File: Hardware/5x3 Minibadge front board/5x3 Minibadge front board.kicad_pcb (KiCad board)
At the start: 2 copper layers, 142.2 x 91.4 mm, 16 parts, among them J1 Board to Board

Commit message: Change board size + mounting holes
still need to finish re-routing the front plate
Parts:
- added J1: Board to Board, Connector_PinHeader_2.54mm:PinHeader_2x05_P2.54mm_Vertical_SMD, B.Cu at (213.4, 96.5)
- added REF**: MountingHole_2.2mm_M2, MountingHole:MountingHole_2.2mm_M2, F.Cu at (92.7, 57.1)
- added REF**: MountingHole_2.2mm_M2, MountingHole:MountingHole_2.2mm_M2, F.Cu at (157.5, 138.4)
- added REF**: MiniBadge_Slot_Reflective, MiniBadge:MiniBadge_Slot_Reflective, F.Cu at (96.6, 61.1)
- added REF**: MountingHole_2.2mm_M2, MountingHole:MountingHole_2.2mm_M2, F.Cu at (92.7, 135.9)
- added REF**: MountingHole_2.2mm_M2, MountingHole:MountingHole_2.2mm_M2, F.Cu at (222.2, 57.1)
- added REF**: MountingHole_2.2mm_M2, MountingHole:MountingHole_2.2mm_M2, F.Cu at (168.9, 54.6)
- added REF**: MountingHole_2.2mm_M2, MountingHole:MountingHole_2.2mm_M2, F.Cu at (146.1, 54.6)
- added REF**: MountingHole_2.2mm_M2, MountingHole:MountingHole_2.2mm_M2, F.Cu at (222.2, 135.9)
- added REF**1: MiniBadge_Slot_Reflective, MiniBadge:MiniBadge_Slot_Reflective, F.Cu at (122.0, 61.1)
- added REF**10: MiniBadge_Slot_Reflective, MiniBadge:MiniBadge_Slot_Reflective, F.Cu at (96.6, 111.9)
- added REF**11: MiniBadge_Slot_Reflective, MiniBadge:MiniBadge_Slot_Reflective, F.Cu at (122.0, 111.9)
- added REF**12: MiniBadge_Slot_Reflective, MiniBadge:MiniBadge_Slot_Reflective, F.Cu at (147.4, 111.9)
- added REF**13: MiniBadge_Slot_Reflective, MiniBadge:MiniBadge_Slot_Reflective, F.Cu at (172.8, 111.9)
- added REF**14: MiniBadge_Slot_Reflective, MiniBadge:MiniBadge_Slot_Reflective, F.Cu at (198.2, 111.9)
- added REF**2: MiniBadge_Slot_Reflective, MiniBadge:MiniBadge_Slot_Reflective, F.Cu at (147.4, 61.1)
- added REF**3: MiniBadge_Slot_Reflective, MiniBadge:MiniBadge_Slot_Reflective, F.Cu at (172.8, 61.1)
- added REF**4: MiniBadge_Slot_Reflective, MiniBadge:MiniBadge_Slot_Reflective, F.Cu at (198.2, 61.1)
- added REF**5: MiniBadge_Slot_Reflective, MiniBadge:MiniBadge_Slot_Reflective, F.Cu at (96.6, 86.5)
- added REF**6: MiniBadge_Slot_Reflective, MiniBadge:MiniBadge_Slot_Reflective, F.Cu at (122.0, 86.5)
- added REF**7: MiniBadge_Slot_Reflective, MiniBadge:MiniBadge_Slot_Reflective, F.Cu at (147.4, 86.5)
- added REF**8: MiniBadge_Slot_Reflective, MiniBadge:MiniBadge_Slot_Reflective, F.Cu at (172.8, 86.5)
- added REF**9: MiniBadge_Slot_Reflective, MiniBadge:MiniBadge_Slot_Reflective, F.Cu at (198.2, 86.5)
- moved MB10 275.1 mm to (444.6, 86.5)
- moved MB15 275.1 mm to (444.6, 110.0)
- moved MB5 275.1 mm to (444.6, 63.0)
- moved J1 275.1 mm to (457.0, 96.5)
- moved MB1 275.1 mm to (348.1, 63.0)
- moved MB11 275.1 mm to (348.1, 110.0)
- moved MB12 275.1 mm to (372.2, 110.0)
- moved MB13 275.1 mm to (396.3, 110.0)
- moved MB2 275.1 mm to (372.2, 63.0)
- moved MB3 275.1 mm to (396.3, 63.0)
- moved MB6 275.1 mm to (348.1, 86.5)
- moved MB7 275.1 mm to (372.2, 86.5)
- moved MB8 275.1 mm to (396.3, 86.5)
- moved MB14 275.1 mm to (420.5, 110.0)
- moved MB4 275.1 mm to (420.5, 63.0)
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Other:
- board size 142.2 x 91.4 mm -> 391.2 x 91.4 mm

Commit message: physical changes
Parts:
- removed the J1 at (457.0, 96.5)
- removed the MB1 at (348.1, 63.0)
- removed the MB10 at (444.6, 86.5)
- removed the MB11 at (348.1, 110.0)
- removed the MB12 at (372.2, 110.0)
- removed the MB13 at (396.3, 110.0)
- removed the MB14 at (420.5, 110.0)
- removed the MB15 at (444.6, 110.0)
- removed the MB2 at (372.2, 63.0)
- removed the MB3 at (396.3, 63.0)
- removed the MB4 at (420.5, 63.0)
- removed the MB5 at (444.6, 63.0)
- removed the MB6 at (348.1, 86.5)
- removed the MB7 at (372.2, 86.5)
- removed the MB8 at (396.3, 86.5)
- removed the MB9 at (420.5, 86.5)
- MB1: renamed from REF**; value MiniBadge_Slot_Reflective -> MiniBadge_Full
- MB10: renamed from REF**9; value MiniBadge_Slot_Reflective -> MiniBadge_Full
- MB11: renamed from REF**10; value MiniBadge_Slot_Reflective -> MiniBadge_Full
- MB12: renamed from REF**11; value MiniBadge_Slot_Reflective -> MiniBadge_Full
- MB13: renamed from REF**12; value MiniBadge_Slot_Reflective -> MiniBadge_Full
- MB14: renamed from REF**13; value MiniBadge_Slot_Reflective -> MiniBadge_Full
- MB15: renamed from REF**14; value MiniBadge_Slot_Reflective -> MiniBadge_Full
- MB2: renamed from REF**1; value MiniBadge_Slot_Reflective -> MiniBadge_Full
- MB3: renamed from REF**2; value MiniBadge_Slot_Reflective -> MiniBadge_Full
- MB4: renamed from REF**3; value MiniBadge_Slot_Reflective -> MiniBadge_Full
- MB5: renamed from REF**4; value MiniBadge_Slot_Reflective -> MiniBadge_Full
- MB6: renamed from REF**5; value MiniBadge_Slot_Reflective -> MiniBadge_Full
- MB7: renamed from REF**6; value MiniBadge_Slot_Reflective -> MiniBadge_Full
- MB8: renamed from REF**7; value MiniBadge_Slot_Reflective -> MiniBadge_Full
- MB9: renamed from REF**8; value MiniBadge_Slot_Reflective -> MiniBadge_Full
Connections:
- J1 pad 1: (no net) -> +3v3-2
- J1 pad 10: (no net) -> GND
- J1 pad 2: (no net) -> +3v3-1
- J1 pad 3: (no net) -> +VBATT
- J1 pad 4: (no net) -> +3v3-3
- J1 pad 5: (no net) -> MB_CLK
- J1 pad 6: (no net) -> +5V
- J1 pad 7: (no net) -> MB_SCL
- J1 pad 8: (no net) -> MB_SDA
- J1 pad 9: (no net) -> GND
- MB1 pad 1: (no net) -> +5V
- MB1 pad 10: (no net) -> unconnected-(MB1-NC-Pad10)
- MB1 pad 11: (no net) -> unconnected-(MB1-NC-Pad11)
- MB1 pad 12: (no net) -> unconnected-(MB1-NC-Pad12)
- MB1 pad 13: (no net) -> MB_SCL
- MB1 pad 14: (no net) -> MB_SDA
- MB1 pad 15: (no net) -> +3v3-1
- MB1 pad 16: (no net) -> GND
- MB1 pad 2: (no net) -> GND
- MB1 pad 3: (no net) -> unconnected-(MB1-PROG1-Pad3)
- MB1 pad 4: (no net) -> unconnected-(MB1-PROG2-Pad4)
- MB1 pad 5: (no net) -> unconnected-(MB1-PROG3-Pad5)
- MB1 pad 6: (no net) -> unconnected-(MB1-PROG4-Pad6)
- MB1 pad 7: (no net) -> +3v3-1
- MB1 pad 8: (no net) -> GND
- MB1 pad 9: (no net) -> MB_CLK
- MB10 pad 1: (no net) -> +5V
- MB10 pad 10: (no net) -> unconnected-(MB10-NC-Pad10)
- MB10 pad 11: (no net) -> unconnected-(MB10-NC-Pad11)
- MB10 pad 12: (no net) -> unconnected-(MB10-NC-Pad12)
- MB10 pad 13: (no net) -> MB_SCL
- MB10 pad 14: (no net) -> MB_SDA
- MB10 pad 15: (no net) -> +3v3-2
- MB10 pad 16: (no net) -> GND
- MB10 pad 2: (no net) -> GND
- MB10 pad 3: (no net) -> unconnected-(MB10-PROG1-Pad3)
- MB10 pad 4: (no net) -> unconnected-(MB10-PROG2-Pad4)
- MB10 pad 5: (no net) -> unconnected-(MB10-PROG3-Pad5)
- MB10 pad 6: (no net) -> unconnected-(MB10-PROG4-Pad6)
- MB10 pad 7: (no net) -> +3v3-2
- MB10 pad 8: (no net) -> GND
- MB10 pad 9: (no net) -> MB_CLK
- MB11 pad 1: (no net) -> +5V
- MB11 pad 10: (no net) -> unconnected-(MB11-NC-Pad10)
- MB11 pad 11: (no net) -> unconnected-(MB11-NC-Pad11)
- MB11 pad 12: (no net) -> unconnected-(MB11-NC-Pad12)
- MB11 pad 13: (no net) -> MB_SCL
- MB11 pad 14: (no net) -> MB_SDA
- MB11 pad 15: (no net) -> +3v3-3
- MB11 pad 16: (no net) -> GND
- MB11 pad 2: (no net) -> GND
- MB11 pad 3: (no net) -> unconnected-(MB11-PROG1-Pad3)
- MB11 pad 4: (no net) -> unconnected-(MB11-PROG2-Pad4)
- MB11 pad 5: (no net) -> unconnected-(MB11-PROG3-Pad5)
- MB11 pad 6: (no net) -> unconnected-(MB11-PROG4-Pad6)
- MB11 pad 7: (no net) -> +3v3-3
- MB11 pad 8: (no net) -> GND
- MB11 pad 9: (no net) -> MB_CLK
- MB12 pad 1: (no net) -> +5V
- MB12 pad 10: (no net) -> unconnected-(MB12-NC-Pad10)
- MB12 pad 11: (no net) -> unconnected-(MB12-NC-Pad11)
- MB12 pad 12: (no net) -> unconnected-(MB12-NC-Pad12)
- MB12 pad 13: (no net) -> MB_SCL
- MB12 pad 14: (no net) -> MB_SDA
- MB12 pad 15: (no net) -> +3v3-3
- MB12 pad 16: (no net) -> GND
- MB12 pad 2: (no net) -> GND
- MB12 pad 3: (no net) -> unconnected-(MB12-PROG1-Pad3)
- MB12 pad 4: (no net) -> unconnected-(MB12-PROG2-Pad4)
- MB12 pad 5: (no net) -> unconnected-(MB12-PROG3-Pad5)
- MB12 pad 6: (no net) -> unconnected-(MB12-PROG4-Pad6)
- MB12 pad 7: (no net) -> +3v3-3
- MB12 pad 8: (no net) -> GND
- MB12 pad 9: (no net) -> MB_CLK
- MB13 pad 1: (no net) -> +5V
- MB13 pad 10: (no net) -> unconnected-(MB13-NC-Pad10)
- MB13 pad 11: (no net) -> unconnected-(MB13-NC-Pad11)
- MB13 pad 12: (no net) -> unconnected-(MB13-NC-Pad12)
- MB13 pad 13: (no net) -> MB_SCL
- MB13 pad 14: (no net) -> MB_SDA
- MB13 pad 15: (no net) -> +3v3-3
- MB13 pad 16: (no net) -> GND
- MB13 pad 2: (no net) -> GND
- MB13 pad 3: (no net) -> unconnected-(MB13-PROG1-Pad3)
- MB13 pad 4: (no net) -> unconnected-(MB13-PROG2-Pad4)
- MB13 pad 5: (no net) -> unconnected-(MB13-PROG3-Pad5)
- MB13 pad 6: (no net) -> unconnected-(MB13-PROG4-Pad6)
- MB13 pad 7: (no net) -> +3v3-3
- MB13 pad 8: (no net) -> GND
- MB13 pad 9: (no net) -> MB_CLK
- MB14 pad 1: (no net) -> +5V
- MB14 pad 10: (no net) -> unconnected-(MB14-NC-Pad10)
- MB14 pad 11: (no net) -> unconnected-(MB14-NC-Pad11)
- MB14 pad 12: (no net) -> unconnected-(MB14-NC-Pad12)
- MB14 pad 13: (no net) -> MB_SCL
- MB14 pad 14: (no net) -> MB_SDA
- MB14 pad 15: (no net) -> +3v3-3
- MB14 pad 16: (no net) -> GND
- MB14 pad 2: (no net) -> GND
- MB14 pad 3: (no net) -> unconnected-(MB14-PROG1-Pad3)
- MB14 pad 4: (no net) -> unconnected-(MB14-PROG2-Pad4)
- MB14 pad 5: (no net) -> unconnected-(MB14-PROG3-Pad5)
- MB14 pad 6: (no net) -> unconnected-(MB14-PROG4-Pad6)
- MB14 pad 7: (no net) -> +3v3-3
- MB14 pad 8: (no net) -> GND
- MB14 pad 9: (no net) -> MB_CLK
- MB15 pad 1: (no net) -> +5V
- MB15 pad 10: (no net) -> unconnected-(MB15-NC-Pad10)
- MB15 pad 11: (no net) -> unconnected-(MB15-NC-Pad11)
- MB15 pad 12: (no net) -> unconnected-(MB15-NC-Pad12)
- MB15 pad 13: (no net) -> MB_SCL
- MB15 pad 14: (no net) -> MB_SDA
- MB15 pad 15: (no net) -> +3v3-3
- MB15 pad 16: (no net) -> GND
- MB15 pad 2: (no net) -> GND
- MB15 pad 3: (no net) -> unconnected-(MB15-PROG1-Pad3)
- MB15 pad 4: (no net) -> unconnected-(MB15-PROG2-Pad4)
- MB15 pad 5: (no net) -> unconnected-(MB15-PROG3-Pad5)
- MB15 pad 6: (no net) -> unconnected-(MB15-PROG4-Pad6)
- MB15 pad 7: (no net) -> +3v3-3
- MB15 pad 8: (no net) -> GND
- MB15 pad 9: (no net) -> MB_CLK
- MB2 pad 1: (no net) -> +5V
- MB2 pad 10: (no net) -> unconnected-(MB2-NC-Pad10)
- MB2 pad 11: (no net) -> unconnected-(MB2-NC-Pad11)
- MB2 pad 12: (no net) -> unconnected-(MB2-NC-Pad12)
- MB2 pad 13: (no net) -> MB_SCL
- MB2 pad 14: (no net) -> MB_SDA
- MB2 pad 15: (no net) -> +3v3-1
- MB2 pad 16: (no net) -> GND
- MB2 pad 2: (no net) -> GND
- MB2 pad 3: (no net) -> unconnected-(MB2-PROG1-Pad3)
- MB2 pad 4: (no net) -> unconnected-(MB2-PROG2-Pad4)
- MB2 pad 5: (no net) -> unconnected-(MB2-PROG3-Pad5)
- MB2 pad 6: (no net) -> unconnected-(MB2-PROG4-Pad6)
- MB2 pad 7: (no net) -> +3v3-1
- MB2 pad 8: (no net) -> GND
- MB2 pad 9: (no net) -> MB_CLK
- MB3 pad 1: (no net) -> +5V
- MB3 pad 10: (no net) -> unconnected-(MB3-NC-Pad10)
- MB3 pad 11: (no net) -> unconnected-(MB3-NC-Pad11)
- MB3 pad 12: (no net) -> unconnected-(MB3-NC-Pad12)
- MB3 pad 13: (no net) -> MB_SCL
- MB3 pad 14: (no net) -> MB_SDA
- MB3 pad 15: (no net) -> +3v3-1
- MB3 pad 16: (no net) -> GND
- MB3 pad 2: (no net) -> GND
- MB3 pad 3: (no net) -> unconnected-(MB3-PROG1-Pad3)
- MB3 pad 4: (no net) -> unconnected-(MB3-PROG2-Pad4)
- MB3 pad 5: (no net) -> unconnected-(MB3-PROG3-Pad5)
- MB3 pad 6: (no net) -> unconnected-(MB3-PROG4-Pad6)
- MB3 pad 7: (no net) -> +3v3-1
- MB3 pad 8: (no net) -> GND
- MB3 pad 9: (no net) -> MB_CLK
- MB4 pad 1: (no net) -> +5V
- MB4 pad 10: (no net) -> unconnected-(MB4-NC-Pad10)
- MB4 pad 11: (no net) -> unconnected-(MB4-NC-Pad11)
- MB4 pad 12: (no net) -> unconnected-(MB4-NC-Pad12)
- MB4 pad 13: (no net) -> MB_SCL
- MB4 pad 14: (no net) -> MB_SDA
- MB4 pad 15: (no net) -> +3v3-1
- MB4 pad 16: (no net) -> GND
- MB4 pad 2: (no net) -> GND
- MB4 pad 3: (no net) -> unconnected-(MB4-PROG1-Pad3)
- MB4 pad 4: (no net) -> unconnected-(MB4-PROG2-Pad4)
- MB4 pad 5: (no net) -> unconnected-(MB4-PROG3-Pad5)
- MB4 pad 6: (no net) -> unconnected-(MB4-PROG4-Pad6)
- MB4 pad 7: (no net) -> +3v3-1
- MB4 pad 8: (no net) -> GND
- MB4 pad 9: (no net) -> MB_CLK
- MB5 pad 1: (no net) -> +5V
- MB5 pad 10: (no net) -> unconnected-(MB5-NC-Pad10)
- MB5 pad 11: (no net) -> unconnected-(MB5-NC-Pad11)
- MB5 pad 12: (no net) -> unconnected-(MB5-NC-Pad12)
- MB5 pad 13: (no net) -> MB_SCL
- MB5 pad 14: (no net) -> MB_SDA
- MB5 pad 15: (no net) -> +3v3-1
- MB5 pad 16: (no net) -> GND
- MB5 pad 2: (no net) -> GND
- MB5 pad 3: (no net) -> unconnected-(MB5-PROG1-Pad3)
- MB5 pad 4: (no net) -> unconnected-(MB5-PROG2-Pad4)
- MB5 pad 5: (no net) -> unconnected-(MB5-PROG3-Pad5)
- MB5 pad 6: (no net) -> unconnected-(MB5-PROG4-Pad6)
- MB5 pad 7: (no net) -> +3v3-1
- MB5 pad 8: (no net) -> GND
- MB5 pad 9: (no net) -> MB_CLK
- MB6 pad 1: (no net) -> +5V
- MB6 pad 10: (no net) -> unconnected-(MB6-NC-Pad10)
- MB6 pad 11: (no net) -> unconnected-(MB6-NC-Pad11)
- MB6 pad 12: (no net) -> unconnected-(MB6-NC-Pad12)
- MB6 pad 13: (no net) -> MB_SCL
- MB6 pad 14: (no net) -> MB_SDA
- MB6 pad 15: (no net) -> +3v3-2
- MB6 pad 16: (no net) -> GND
- MB6 pad 2: (no net) -> GND
- MB6 pad 3: (no net) -> unconnected-(MB6-PROG1-Pad3)
- MB6 pad 4: (no net) -> unconnected-(MB6-PROG2-Pad4)
- MB6 pad 5: (no net) -> unconnected-(MB6-PROG3-Pad5)
- MB6 pad 6: (no net) -> unconnected-(MB6-PROG4-Pad6)
- MB6 pad 7: (no net) -> +3v3-2
- MB6 pad 8: (no net) -> GND
- MB6 pad 9: (no net) -> MB_CLK
- MB7 pad 1: (no net) -> +5V
- MB7 pad 10: (no net) -> unconnected-(MB7-NC-Pad10)
- MB7 pad 11: (no net) -> unconnected-(MB7-NC-Pad11)
- MB7 pad 12: (no net) -> unconnected-(MB7-NC-Pad12)
- MB7 pad 13: (no net) -> MB_SCL
- MB7 pad 14: (no net) -> MB_SDA
- MB7 pad 15: (no net) -> +3v3-2
- MB7 pad 16: (no net) -> GND
- MB7 pad 2: (no net) -> GND
- MB7 pad 3: (no net) -> unconnected-(MB7-PROG1-Pad3)
- MB7 pad 4: (no net) -> unconnected-(MB7-PROG2-Pad4)
- MB7 pad 5: (no net) -> unconnected-(MB7-PROG3-Pad5)
- MB7 pad 6: (no net) -> unconnected-(MB7-PROG4-Pad6)
- MB7 pad 7: (no net) -> +3v3-2
- MB7 pad 8: (no net) -> GND
- MB7 pad 9: (no net) -> MB_CLK
- MB8 pad 1: (no net) -> +5V
- MB8 pad 10: (no net) -> unconnected-(MB8-NC-Pad10)
- MB8 pad 11: (no net) -> unconnected-(MB8-NC-Pad11)
- MB8 pad 12: (no net) -> unconnected-(MB8-NC-Pad12)
- MB8 pad 13: (no net) -> MB_SCL
- MB8 pad 14: (no net) -> MB_SDA
- MB8 pad 15: (no net) -> +3v3-2
- MB8 pad 16: (no net) -> GND
- MB8 pad 2: (no net) -> GND
- MB8 pad 3: (no net) -> unconnected-(MB8-PROG1-Pad3)
- MB8 pad 4: (no net) -> unconnected-(MB8-PROG2-Pad4)
- MB8 pad 5: (no net) -> unconnected-(MB8-PROG3-Pad5)
- MB8 pad 6: (no net) -> unconnected-(MB8-PROG4-Pad6)
- MB8 pad 7: (no net) -> +3v3-2
- MB8 pad 8: (no net) -> GND
- MB8 pad 9: (no net) -> MB_CLK
- MB9 pad 1: (no net) -> +5V
- MB9 pad 10: (no net) -> unconnected-(MB9-NC-Pad10)
- MB9 pad 11: (no net) -> unconnected-(MB9-NC-Pad11)
- MB9 pad 12: (no net) -> unconnected-(MB9-NC-Pad12)
- MB9 pad 13: (no net) -> MB_SCL
- MB9 pad 14: (no net) -> MB_SDA
- MB9 pad 15: (no net) -> +3v3-2
- MB9 pad 16: (no net) -> GND
- MB9 pad 2: (no net) -> GND
- MB9 pad 3: (no net) -> unconnected-(MB9-PROG1-Pad3)
- MB9 pad 4: (no net) -> unconnected-(MB9-PROG2-Pad4)
- MB9 pad 5: (no net) -> unconnected-(MB9-PROG3-Pad5)
- MB9 pad 6: (no net) -> unconnected-(MB9-PROG4-Pad6)
- MB9 pad 7: (no net) -> +3v3-2
- MB9 pad 8: (no net) -> GND
- MB9 pad 9: (no net) -> MB_CLK
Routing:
- net MB_CLK: track 420.5 -> 0.00 mm
- net MB_SCL: track 417.3 -> 0.00 mm, vias 16 -> 0
- net MB_SDA: track 395.2 -> 0.00 mm, vias 16 -> 0
- net +5V: track 391.5 -> 0.00 mm, vias 1 -> 0
- net GND: track 272.1 -> 0.00 mm, vias 12 -> 0
- net +3v3-1: track 237.4 -> 0.00 mm, vias 1 -> 0
- net +3v3-3: track 218.4 -> 0.00 mm, vias 2 -> 0
- net +3v3-2: track 205.1 -> 0.00 mm, vias 2 -> 0
- removed copper zone on B.Cu, net GND
- removed copper zone on F.Cu, net GND
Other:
- board size 391.2 x 91.4 mm -> 142.2 x 91.4 mm
- board text removed: "+3V3-1 +3V3-3 +5V MB_SDA GND"
- board text removed: "+3V3-2 +VBATT MB_CLK MB_SCL GND"

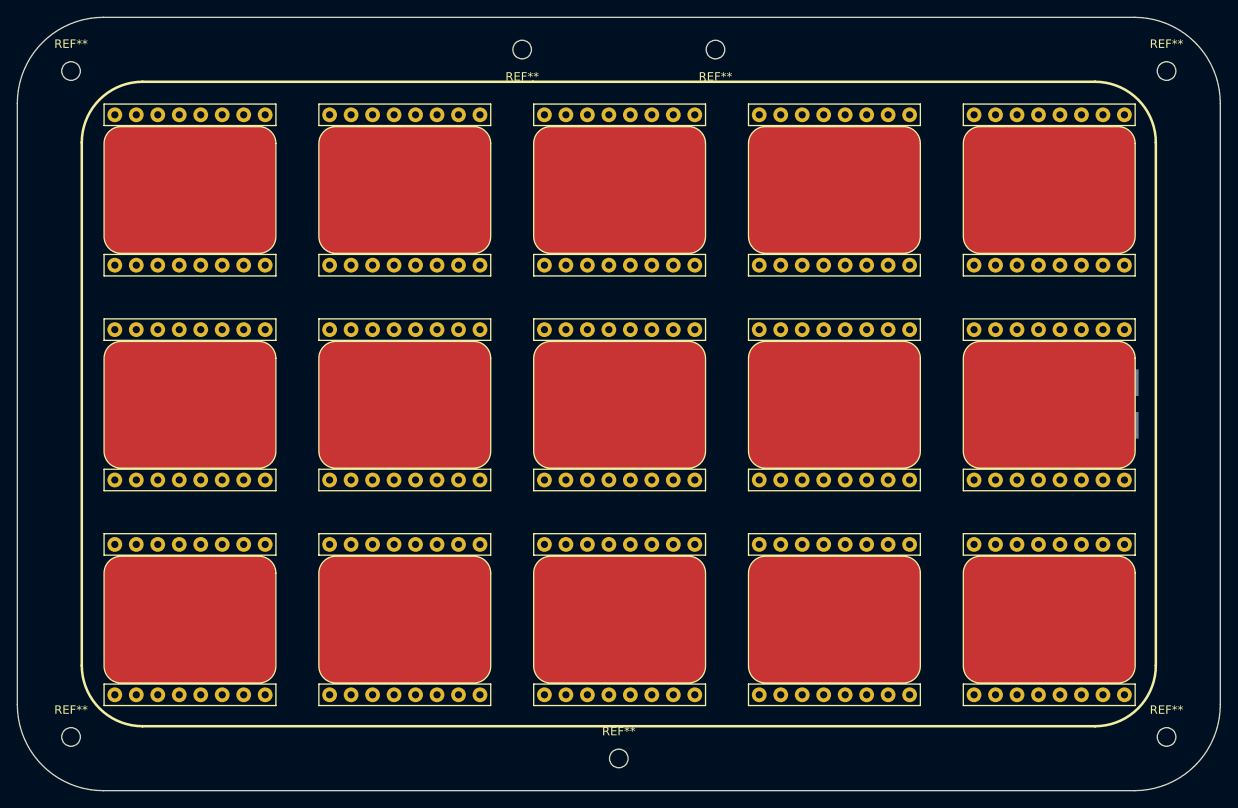
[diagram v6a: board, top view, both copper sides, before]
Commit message: re-routed front minibadge board
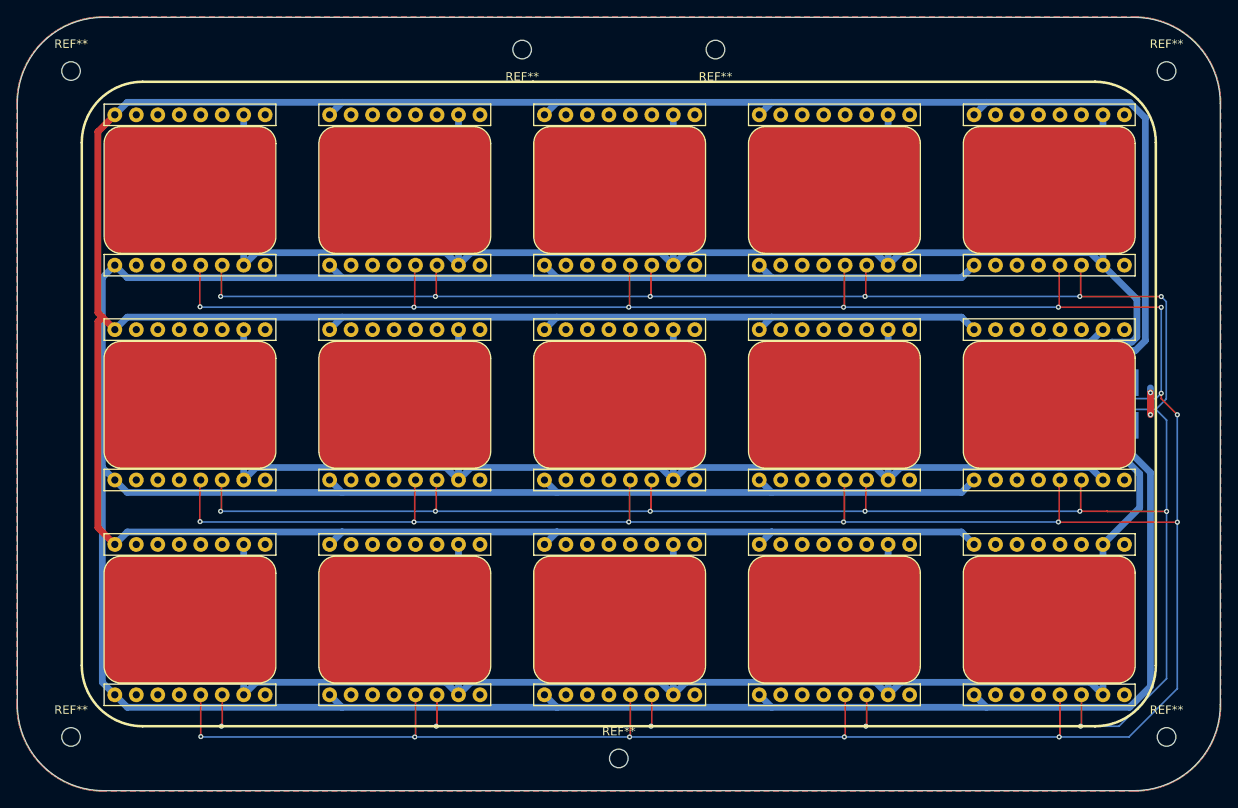
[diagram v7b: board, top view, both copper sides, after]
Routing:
- net MB_SCL: track 0.00 -> 475.0 mm, vias 0 -> 19
- net MB_CLK: track 0.00 -> 447.3 mm
- net MB_SDA: track 0.00 -> 445.8 mm, vias 0 -> 17
- net +5V: track 0.00 -> 445.1 mm
- net +3v3-1: track 0.00 -> 226.1 mm
- net +3v3-3: track 0.00 -> 218.0 mm
- net +3v3-2: track 0.00 -> 211.0 mm
- net GND: track 0.00 -> 3.18 mm, vias 0 -> 2
- added copper zone on B.Cu, net GND
- added copper zone on F.Cu, net GND

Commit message: front board initial silkscreen
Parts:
- added G***: LOGO, LOGO, B.Cu at (115.4, 96.8)
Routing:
- net +5V: track 445.1 -> 450.0 mm
- net MB_CLK: track 447.3 -> 450.7 mm
- net +3v3-1: track 226.1 -> 228.6 mm
- net +3v3-2: track 211.0 -> 213.2 mm
- net MB_SDA: track 445.8 -> 447.1 mm
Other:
- board text added: "${TITLE}"
- board text added: "+3v3-1 +3v3-3 +5V SDA GND"
- board text added: "+3v3-2 +VBATT CLK SCL GND"
- board text added: "5 x 3 Rechargable Minibadge display"
- board text added: "Pips801"
